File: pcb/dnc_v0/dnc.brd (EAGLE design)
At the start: 100 x 83.2 mm, 70 parts, among them Q5 TSM2306CX, Q7 TSM2306CX, Q8 TSM2306CX

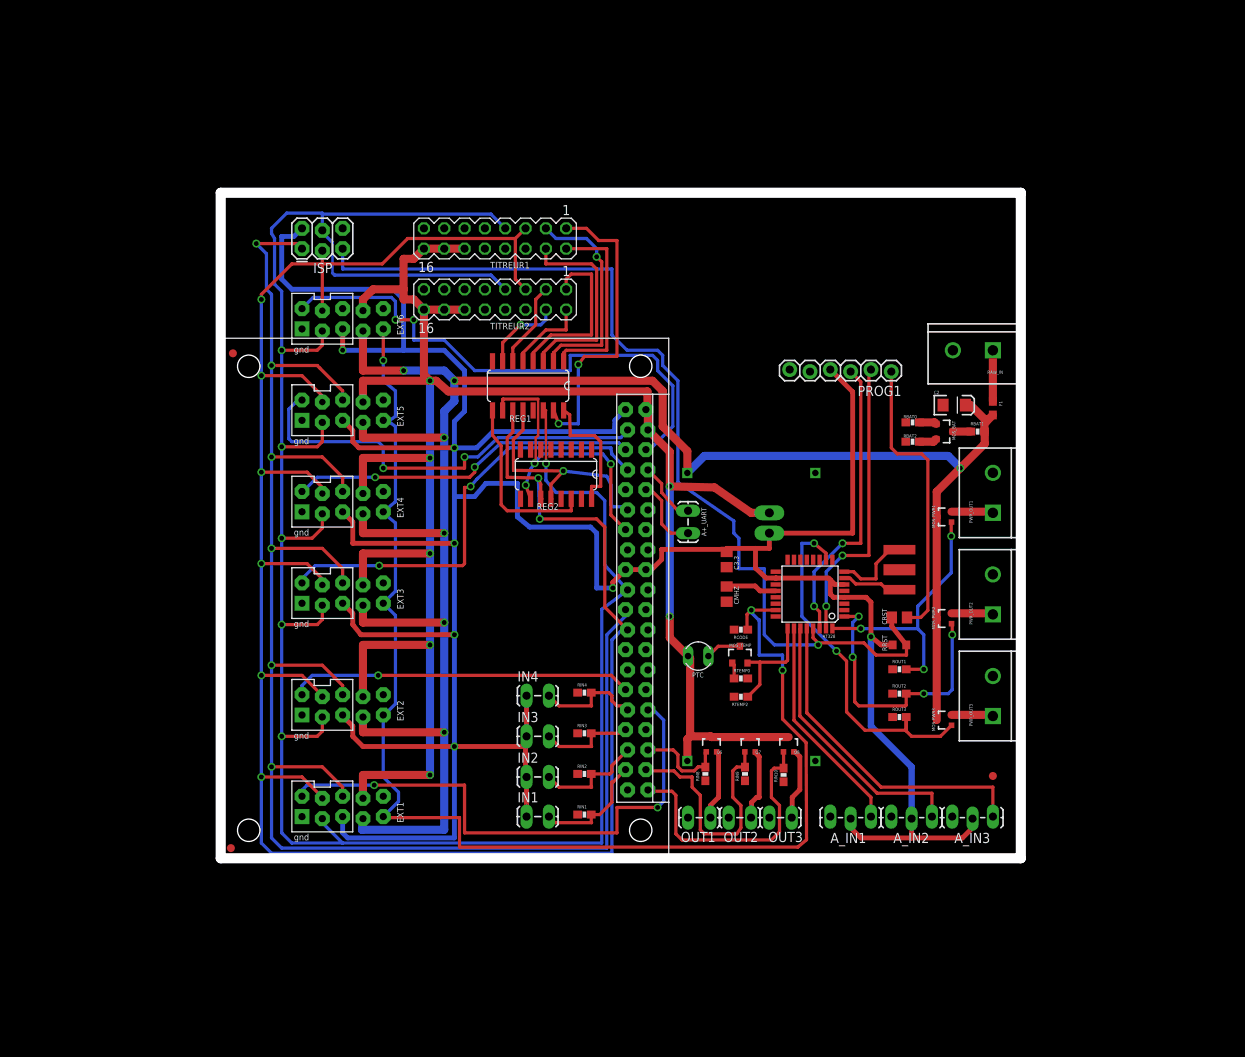
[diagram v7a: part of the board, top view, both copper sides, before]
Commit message: Route finished, first version
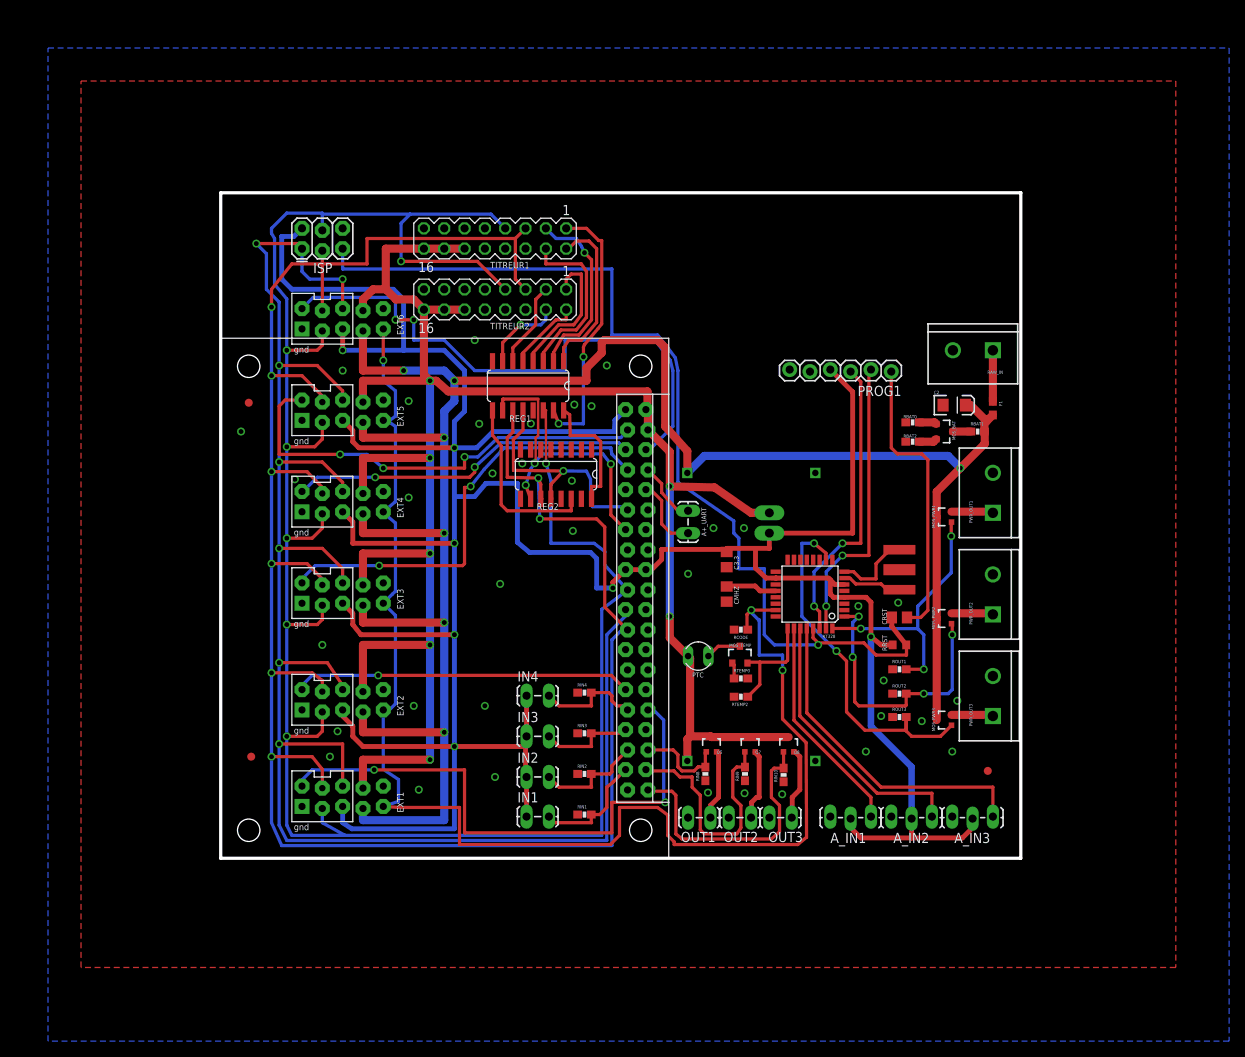
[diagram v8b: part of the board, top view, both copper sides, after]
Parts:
- moved JP13 11.7 mm to (3.81, 12.7)
- moved JP19 6.49 mm to (3.51, 56.9)
- moved EXT1 1.27 mm to (15.2, 7.62)
- moved JP14 0.90 mm to (95.9, 10.9)
- moved EXT2 0.63 mm to (15.2, 19.7)
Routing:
- net MOSI: track 281.4 -> 270.3 mm, vias 6 -> 7
- net CODE: track 164.4 -> 173.1 mm
- net RAW: track 252.6 -> 261.1 mm
- net MISO: track 211.2 -> 218.5 mm, vias 6 -> 7
- net SCK: track 281.3 -> 275.2 mm
- net RST1: track 38.5 -> 33.7 mm
- net RST3: track 27.2 -> 23.1 mm
- net RST4: track 25.8 -> 21.8 mm
- net RST5: track 21.6 -> 17.8 mm
- net /CS_EXT_6: track 67.4 -> 71.2 mm
- net RST2: track 24.4 -> 21.2 mm
- net /CS_EXT_1: track 68.4 -> 71.3 mm
- net /CS_EXT_5: track 54.0 -> 56.2 mm, vias 2 -> 3
- net N$44: track 8.03 -> 10.1 mm
- net N$43: track 5.80 -> 7.54 mm
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- added copper zone on layer 1, net GND
- added copper zone on layer 16, net GND
